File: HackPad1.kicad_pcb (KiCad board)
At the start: 2 copper layers, 60 x 60 mm, 9 parts, among them SW1 SW_SPDT, U1 ATtiny85V-10P

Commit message: design
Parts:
- moved BT1 3.91 mm to (121.0, 97.5)
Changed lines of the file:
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@@
 	(footprint "Battery:BatteryHolder_Keystone_104_1x23mm"
 		(layer "F.Cu")
-		(at 117.23 98.5)
+		(at 121.01 97.5)
 		(descr "http://www.keyelco.com/product-pdf.cfm?p=744")
 		(tags "Keystone type 104 battery holder")

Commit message: design 2
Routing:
- net /MIC: track 32.8 -> 35.4 mm
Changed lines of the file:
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@@
+	)
+	(segment
+		(start 117.5 92.5)
+		(end 110.35 85.35)
+		(width 0.3)
+		(layer "F.Cu")
+		(net 1)
+	)
+	(segment
+		(start 131.72 92.5)
+		(end 117.5 92.5)
+		(width 0.3)
+		(layer "F.Cu")
+		(net 1)
+	)
+	(segment
+		(start 137.72 98.5)
+		(end 131.72 92.5)
+		(width 0.3)
+		(layer "F.Cu")
+		(net 1)
 	)
 	(segment
@@
 	)
 	(segment
-		(start 110.5 85.5)
-		(end 110.35 85.35)
-		(width 0.3)
-		(layer "F.Cu")
-		(net 1)
-	)
-	(segment
-		(start 124.72 85.5)
-		(end 110.5 85.5)
-		(width 0.3)
-		(layer "F.Cu")
-		(net 1)
-	)
-	(segment
-		(start 137.72 98.5)
-		(end 124.72 85.5)
-		(width 0.3)
-		(layer "F.Cu")
-		(net 1)
-	)
-	(segment
 		(start 117.23 98.27)
 		(end 117.5 98)
@@
 	)
 	(segment
-		(start 126.5 67.94)
+		(start 126.5 63.5)
+		(end 126.76 63.24)
+		(width 0.3)
+		(layer "F.Cu")
+		(net 5)
+	)
+	(segment
+		(start 126.76 63.24)
 		(end 131.2 63.24)
 		(width 0.3)
@@
 	(segment
 		(start 126.5 75.5)
-		(end 126.5 67.94)
+		(end 126.5 63.5)
 		(width 0.3)
 		(layer "F.Cu")
@@
 	)
 	(segment
-		(start 124.02 75.5)
-		(end 131.2 68.32)
-		(width 0.5)
-		(layer "B.Cu")
-		(net 6)
-	)
-	(segment
-		(start 116.5 75.5)
-		(end 124.02 75.5)
-		(width 0.5)
-		(layer "B.Cu")
-		(net 6)
-	)
-	(segment
 		(start 131.2 68.32)
 		(end 137.88 75)
@@
 		(width 0.5)
 		(layer "B.Cu")
+		(net 6)
+	)
+	(segment
+		(start 116.5 75.5)
+		(end 120.5 71.5)
+		(width 0.5)
+		(layer "B.Cu")
+		(net 6)
+	)
+	(segment
+		(start 128.02 71.5)
+		(end 131.2 68.32)
+		(width 0.5)
+		(layer "B.Cu")
+		(net 6)
+	)
+	(segment
+		(start 120.5 71.5)
+		(end 128.02 71.5)
+		(width 0.5)
+		(layer "B.Cu")

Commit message: design 3
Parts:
- moved D1 6.80 mm to (148.7, 92.3)
- moved BT1 3.16 mm to (118.2, 99.0)
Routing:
- net Net-(D1-K): track 24.9 -> 33.4 mm
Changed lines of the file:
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@@
 	(footprint "LED_THT:LED_D3.0mm_Horizontal_O1.27mm_Z2.0mm_IRGrey"
 		(layer "F.Cu")
-		(at 146.665 85.77 90)
+		(at 148.665 92.27 90)
 		(descr "LED, diameter 3.0mm, horizontal offset 1.27mm, z-position of LED center 2.0mm, 2 pins, infrared, grey, generated by kicad-footprint-generator")
 		(tags "LED IR")
@@
 	(footprint "Battery:BatteryHolder_Keystone_104_1x23mm"
 		(layer "F.Cu")
-		(at 121.01 97.5)
+		(at 118.23 99)
 		(descr "http://www.keyelco.com/product-pdf.cfm?p=744")
 		(tags "Keystone type 104 battery holder")
@@
 	)
 	(segment
-		(start 145 84.105)
-		(end 146.665 85.77)
+		(start 145 78.5)
+		(end 145 84.5)
+		(width 0.3)
+		(layer "F.Cu")
+		(net 4)
+	)
+	(segment
+		(start 145 84.5)
+		(end 149 88.5)
+		(width 0.3)
+		(layer "F.Cu")
+		(net 4)
+	)
+	(segment
+		(start 149.915 89.212233)
+		(end 149.202767 88.5)
+		(width 0.3)
+		(layer "F.Cu")
+		(net 4)
+	)
+	(segment
+		(start 130.15 76.15)
+		(end 132 78)
+		(width 0.3)
+		(layer "F.Cu")
+		(net 4)
+	)
+	(segment
+		(start 148.665 92.27)
+		(end 149.915 91.02)
+		(width 0.3)
+		(layer "F.Cu")
+		(net 4)
+	)
+	(segment
+		(start 132 78)
+		(end 144.5 78)
+		(width 0.3)
+		(layer "F.Cu")
+		(net 4)
+	)
+	(segment
+		(start 149.202767 88.5)
+		(end 149 88.5)
+		(width 0.3)
+		(layer "F.Cu")
+		(net 4)
+	)
+	(segment
+		(start 149.915 91.02)
+		(end 149.915 89.212233)
 		(width 0.3)
 		(layer "F.Cu")
@@
 		(width 0.3)
 		(layer "F.Cu")
-		(net 4)
-	)
-	(segment
-		(start 145 78.5)
-		(end 145 84.105)
-		(width 0.3)
-		(layer "F.Cu")
-		(net 4)
-	)
-	(segment
-		(start 130.15 76.15)
-		(end 132 78)
-		(width 0.3)
-		(layer "F.Cu")
-		(net 4)
-	)
-	(segment
-		(start 132 78)
-		(end 144.5 78)
-		(width 0.3)
-		(layer "F.Cu")

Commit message: design 4
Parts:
- moved BT1 7.43 mm to (111.2, 96.5)
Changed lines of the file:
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@@
 	(footprint "Battery:BatteryHolder_Keystone_104_1x23mm"
 		(layer "F.Cu")
-		(at 118.23 99)
+		(at 111.23 96.5)
 		(descr "http://www.keyelco.com/product-pdf.cfm?p=744")
 		(tags "Keystone type 104 battery holder")

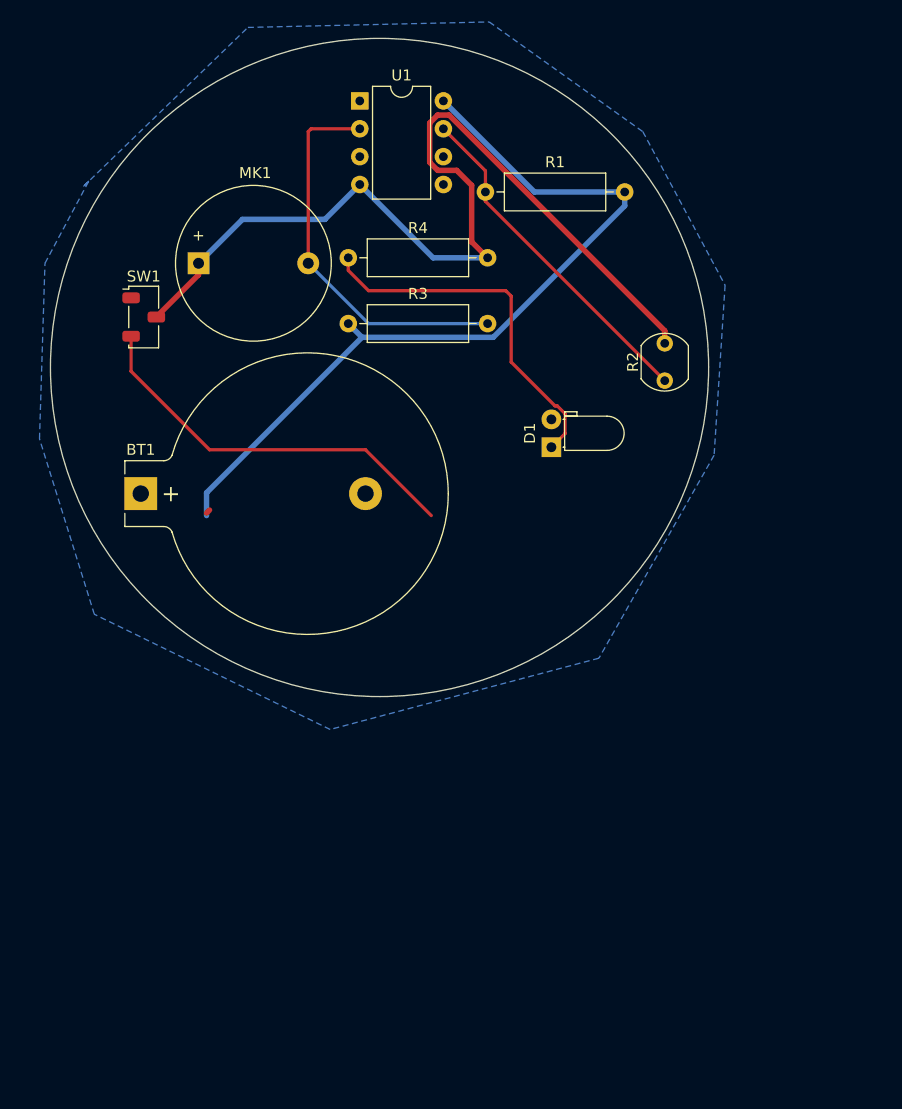
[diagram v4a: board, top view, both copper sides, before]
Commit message: added all footprints
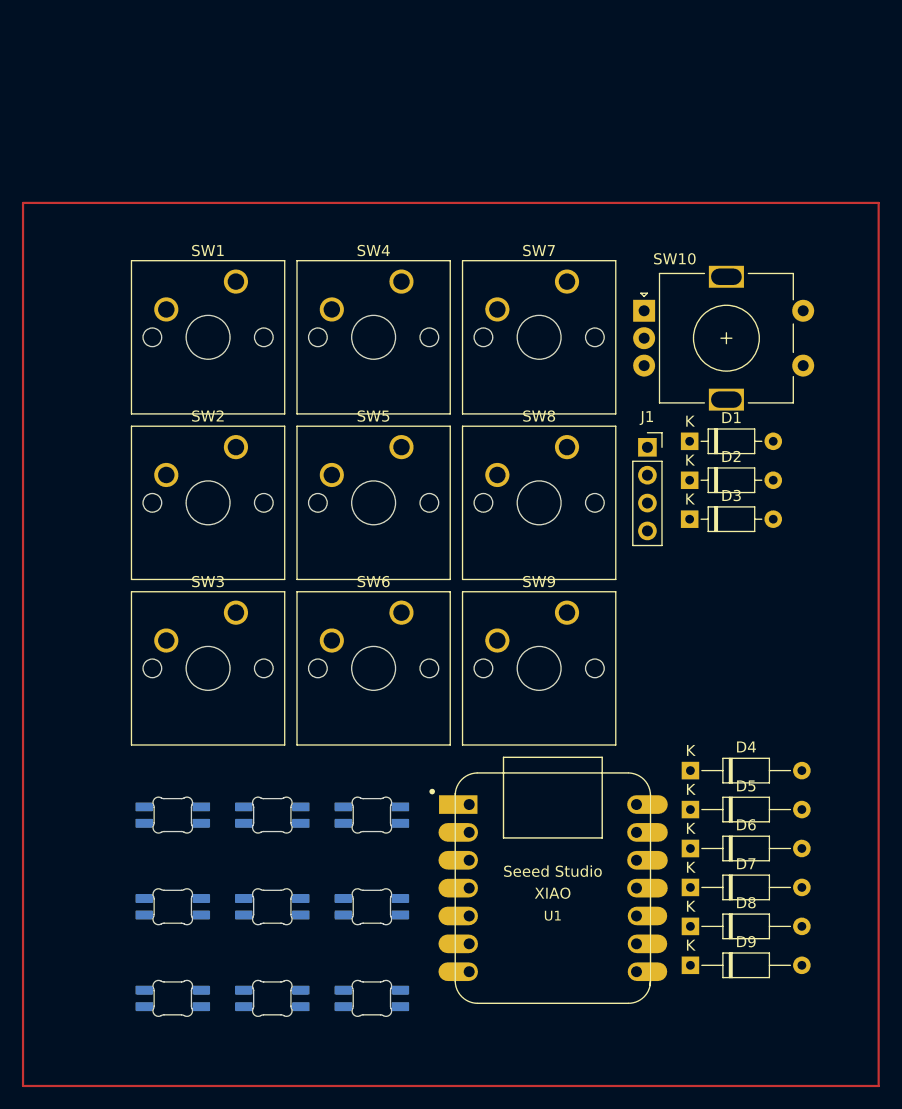
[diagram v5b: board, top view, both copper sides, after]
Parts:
- removed BT1: 3.3V Cell, Battery:BatteryHolder_Keystone_104_1x23mm
- removed MK1: Microphone_Condenser, Buzzer_Beeper:Buzzer_D14mm_H7mm_P10mm
- removed R1, R3, R4: R, Resistor_THT:R_Axial_DIN0309_L9.0mm_D3.2mm_P12.70mm_Horizontal
- removed R2: LDR07, OptoDevice:R_LDR_5.1x4.3mm_P3.4mm_Vertical
- added D10: WS2812B, Keyboard_Parts:MX_SK6812MINI-E, F.Cu at (114.2, 120.7)
- added D11: WS2812B, Keyboard_Parts:MX_SK6812MINI-E, F.Cu at (114.2, 129.1)
- added D12: WS2812B, Keyboard_Parts:MX_SK6812MINI-E, F.Cu at (114.2, 137.4)
- added D13: WS2812B, Keyboard_Parts:MX_SK6812MINI-E, F.Cu at (123.2, 120.7)
- added D14: WS2812B, Keyboard_Parts:MX_SK6812MINI-E, F.Cu at (123.2, 129.1)
- added D15: WS2812B, Keyboard_Parts:MX_SK6812MINI-E, F.Cu at (123.2, 137.4)
- added D16: WS2812B, Keyboard_Parts:MX_SK6812MINI-E, F.Cu at (132.3, 120.7)
- added D17: WS2812B, Keyboard_Parts:MX_SK6812MINI-E, F.Cu at (132.3, 129.1)
- added D18: WS2812B, Keyboard_Parts:MX_SK6812MINI-E, F.Cu at (132.3, 137.4)
- added D2: D, Diode_THT:D_DO-35_SOD27_P7.62mm_Horizontal, F.Cu at (161.3, 95.3)
- added D3: D, Diode_THT:D_DO-35_SOD27_P7.62mm_Horizontal, F.Cu at (161.3, 98.8)
- added D4: D, Diode_THT:D_DO-35_SOD27_P10.16mm_Horizontal, F.Cu at (161.3, 121.8)
- added D5: D, Diode_THT:D_DO-35_SOD27_P10.16mm_Horizontal, F.Cu at (161.3, 125.3)
- added D6: D, Diode_THT:D_DO-35_SOD27_P10.16mm_Horizontal, F.Cu at (161.3, 128.8)
- added D7: D, Diode_THT:D_DO-35_SOD27_P10.16mm_Horizontal, F.Cu at (161.3, 132.4)
- added D8: D, Diode_THT:D_DO-35_SOD27_P10.16mm_Horizontal, F.Cu at (161.3, 135.9)
- added D9: D, Diode_THT:D_DO-35_SOD27_P10.16mm_Horizontal, F.Cu at (161.3, 139.5)
- added J1: Conn_01x04_Pin, Connector_PinSocket_2.54mm:PinSocket_1x04_P2.54mm_Vertical, F.Cu at (157.4, 92.3)
- added SW10: RotaryEncoder, Rotary_Encoder:RotaryEncoder_Alps_EC11E-Switch_Vertical_H20mm, F.Cu at (157.1, 79.8)
- added SW2: SW_Push, Button_Switch_Keyboard:SW_Cherry_MX_1.00u_PCB, F.Cu at (119.9, 92.3)
- added SW3: SW_Push, Button_Switch_Keyboard:SW_Cherry_MX_1.00u_PCB, F.Cu at (119.9, 107.3)
- added SW4: SW_Push, Button_Switch_Keyboard:SW_Cherry_MX_1.00u_PCB, F.Cu at (135.0, 77.2)
- added SW5: SW_Push, Button_Switch_Keyboard:SW_Cherry_MX_1.00u_PCB, F.Cu at (135.0, 92.3)
- added SW6: SW_Push, Button_Switch_Keyboard:SW_Cherry_MX_1.00u_PCB, F.Cu at (135.0, 107.3)
- added SW7: SW_Push, Button_Switch_Keyboard:SW_Cherry_MX_1.00u_PCB, F.Cu at (150.1, 77.2)
- added SW8: SW_Push, Button_Switch_Keyboard:SW_Cherry_MX_1.00u_PCB, F.Cu at (150.1, 92.3)
- added SW9: SW_Push, Button_Switch_Keyboard:SW_Cherry_MX_1.00u_PCB, F.Cu at (150.1, 107.3)
- D1: value LED -> D; footprint LED_THT:LED_D3.0mm_Horizontal_O1.27mm_Z2.0mm_IRGrey -> Diode_THT:D_DO-35_SOD27_P7.62mm_Horizontal
- SW1: value SW_SPDT -> SW_Push; footprint Button_Switch_SMD:Nidec_Copal_CAS-120A -> Button_Switch_Keyboard:SW_Cherry_MX_1.00u_PCB
- U1: value ATtiny85V-10P -> MOUDLE-SEEEDUINO-XIAO; footprint Package_DIP:DIP-8_W7.62mm -> footprints:XIAO-Generic-Hybrid-14P-2.54-21X17.8MM
- moved U1 73.9 mm to (148.8, 132.5)
- moved D1 12.6 mm to (161.3, 91.7), turned to 0 degrees
- moved SW1 9.01 mm to (119.9, 77.2)
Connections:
- D1 pad 1: Net-(D1-K) -> COL1
- D1 pad 2: unconnected-(D1-A-Pad2) -> Net-(D1-A)
- SW1 pad 1: unconnected-(SW1-A-Pad1) -> ROW1
- SW1 pad 2: GND -> Net-(D1-A)
- U1 pad 1: unconnected-(U1-~{RESET}/PB5-Pad1) -> COL1
- U1 pad 2: /MIC -> COL2
- U1 pad 3: unconnected-(U1-XTAL2/PB4-Pad3) -> COL3
- U1 pad 4: GND -> ROW1
- U1 pad 5: unconnected-(U1-AREF/PB0-Pad5) -> SDA
- U1 pad 6: /LED -> SCL
- U1 pad 7: /LDR -> ROW2
- U1 pad 8: +3.3V -> ROW3
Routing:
- net GND: track 85.1 -> 0.00 mm
- net +3.3V: track 74.4 -> 0.00 mm
- net Net-(BT1--): track 36.0 -> 0.00 mm
- net /MIC: track 35.4 -> 0.00 mm
- net Net-(D1-K): track 33.4 -> 0.00 mm
- net /LDR: track 31.3 -> 0.00 mm
- removed copper zone on B.Cu, net GND
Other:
- board size 60 x 60 mm -> 3.6 x 3.3 mm

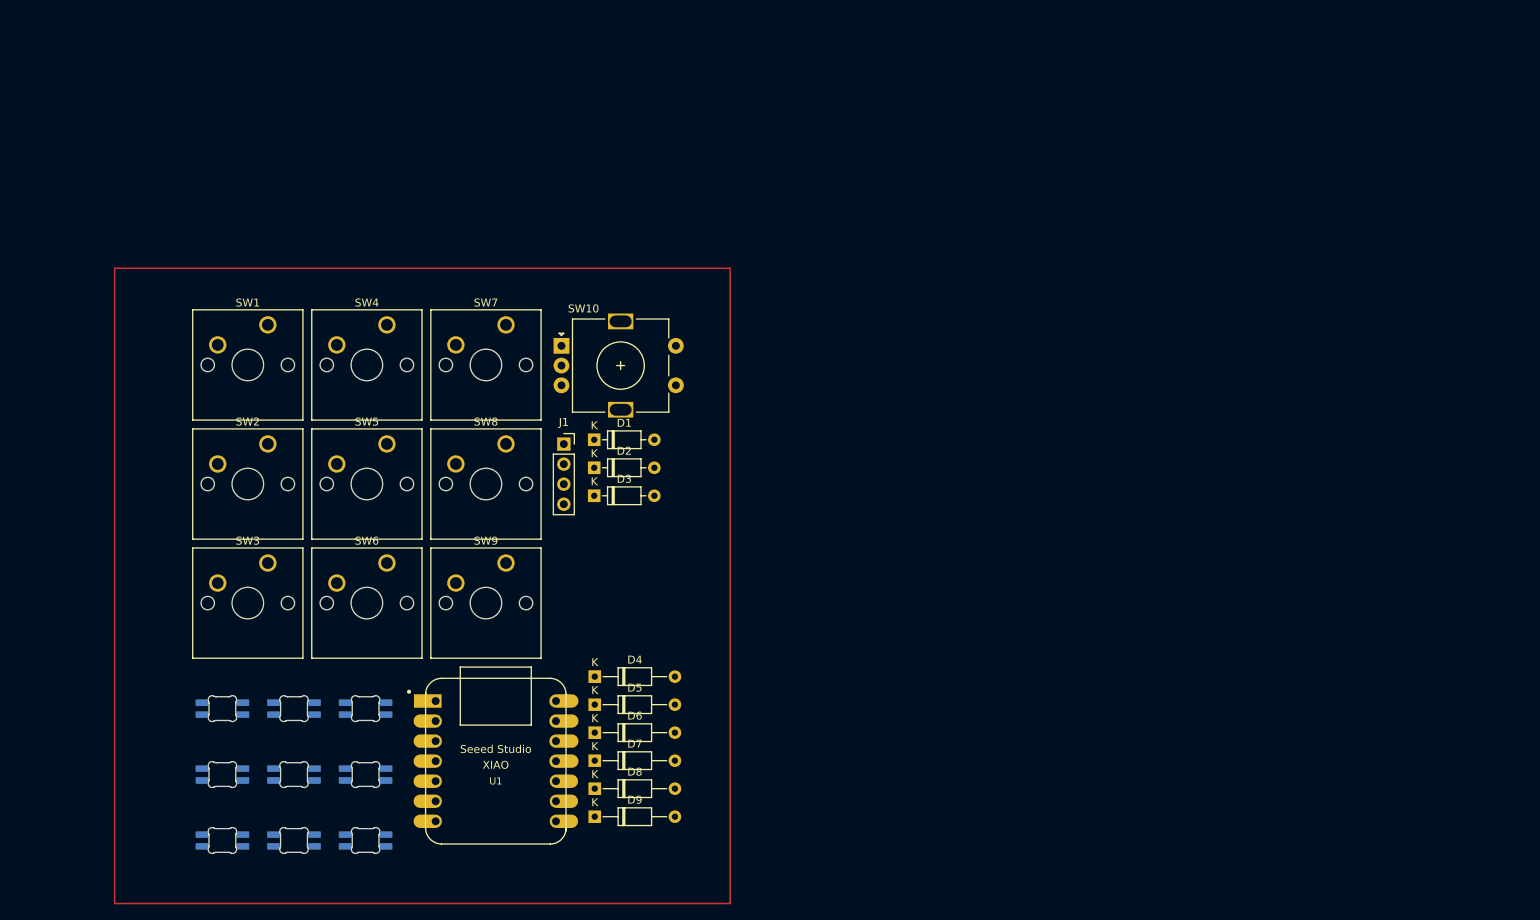
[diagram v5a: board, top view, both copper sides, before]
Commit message: updated switch pcb layout
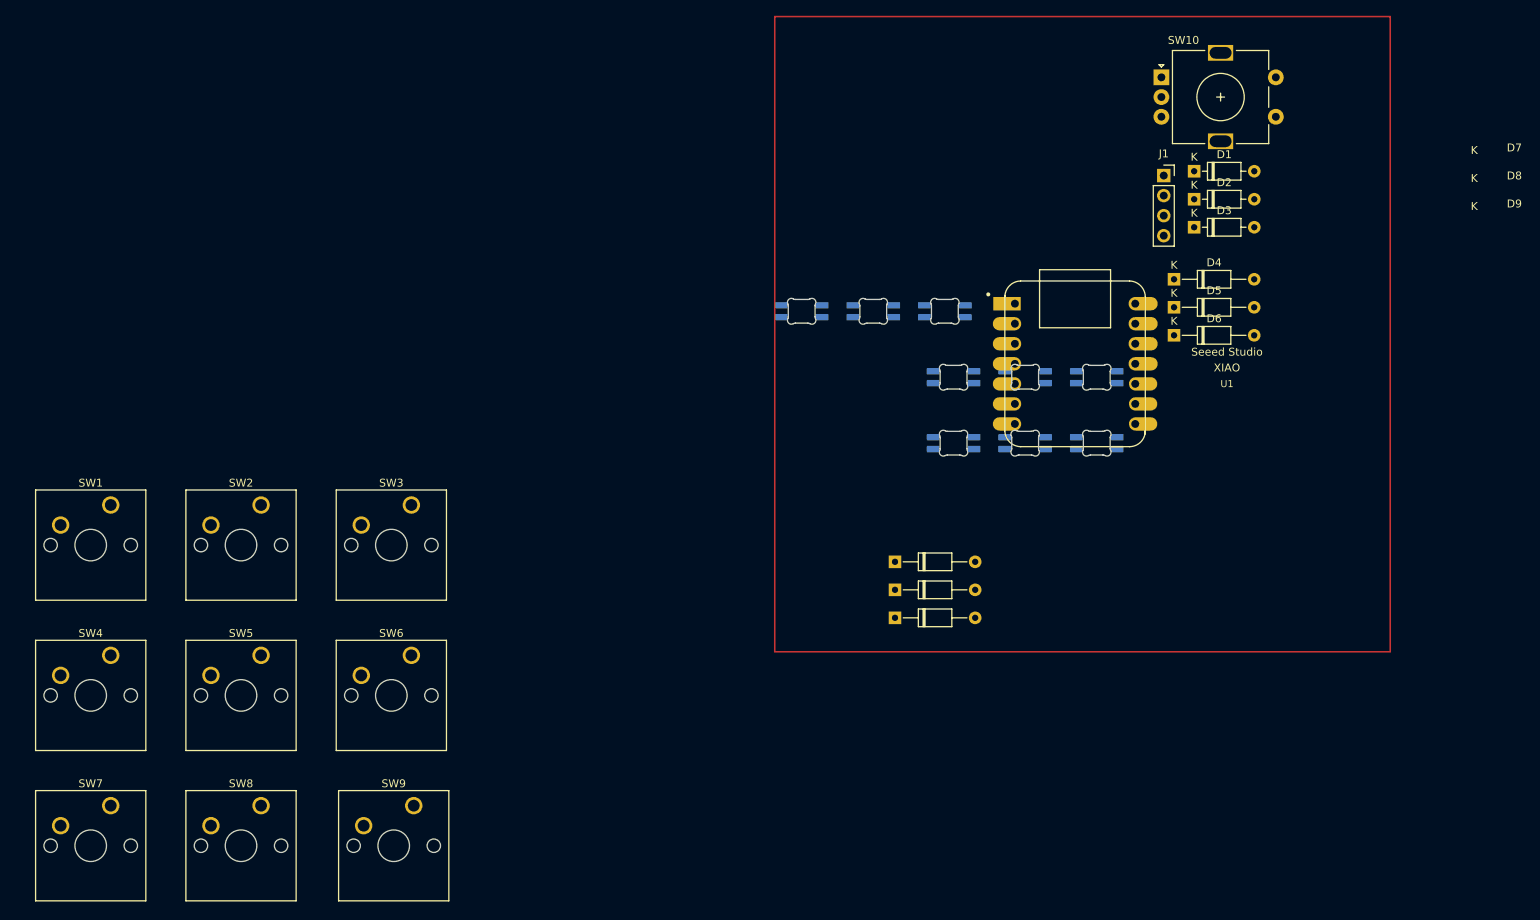
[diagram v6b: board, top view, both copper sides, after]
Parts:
- moved D11 105.5 mm to (206.8, 78.7)
- moved D12 105.5 mm to (206.8, 87.1)
- moved D14 105.5 mm to (215.9, 78.7)
- moved D15 105.5 mm to (215.9, 87.1)
- moved D17 105.5 mm to (225.0, 78.7)
- moved D18 105.5 mm to (225.0, 87.1)
- moved D4 89.0 mm to (234.8, 71.4)
- moved D10 89.0 mm to (187.6, 70.4)
- moved D13 89.0 mm to (196.6, 70.4)
- moved D16 89.0 mm to (205.7, 70.4)
- moved D5 89.0 mm to (234.8, 74.9)
- moved D6 89.0 mm to (234.8, 78.5)
- moved U1 89.0 mm to (222.2, 82.1)
- moved D1 83.3 mm to (237.3, 57.7)
- moved D2 83.3 mm to (237.3, 61.2)
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
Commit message: designed led pcb layout
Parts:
- removed D14, D15, D16, D17, D18: WS2812B, Keyboard_Parts:MX_SK6812MINI-E
- D1, D2, D3, D4, D5, D6, D7, D8, D9: moved to B.Cu
- moved D1 141.3 mm to (101.0, 95.0), turned to 180 degrees
- moved D4 139.7 mm to (102.1, 115.0), turned to 180 degrees
- moved D2 122.4 mm to (119.6, 95.0), turned to 180 degrees
- moved D5 120.4 mm to (121.2, 115.0), turned to 180 degrees
- moved D13 114.2 mm to (102.0, 134.2), turned to 90 degrees
- moved D3 102.1 mm to (139.8, 95.0), turned to 180 degrees
- moved D6 101.4 mm to (140.2, 115.0), turned to 180 degrees
- moved D7 100.9 mm to (102.1, 134.0), turned to 180 degrees
- moved D12 97.8 mm to (121.2, 134.2), turned to 90 degrees
- moved D10 96.4 mm to (101.8, 114.5), turned to 90 degrees
- moved D11 92.8 mm to (121.1, 114.2), turned to 90 degrees
- moved D8 81.8 mm to (121.0, 134.0), turned to 180 degrees
- moved D9 62.5 mm to (140.1, 134.0), turned to 180 degrees
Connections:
- D13 pad 2: Net-(D13-DOUT) -> unconnected-(D13-DOUT-Pad2)
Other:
- board size 3.6 x 3.3 mm -> 3.3 x 3.6 mm
